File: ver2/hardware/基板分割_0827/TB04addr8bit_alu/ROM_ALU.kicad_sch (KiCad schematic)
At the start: 31 parts, among them IC601 74HC161N, J601 Conn_02x05_Odd_Even, SW601 SW_Coded_SH-7050, U601 74LS273, U602 74HC273, U603 28C256, U604 28C256, U605 74HC74, U606 74HC273, U607 74HC238

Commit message: ver2: 3分割で他基板側のICを削除(ctrl 9・alu 15・if 2個)
削除前にまたぎ本数(37/20)で割り当てを検算。kicad-cliのパース通過を確認。

Co-Authored-By: Claude Opus 5 <noreply@anthropic.com>
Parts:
- removed IC601: 74HC161N, Package_DIP:DIP-16_W7.62mm_Socket, symbol 74HC161:74HC161N
- removed U601: 74LS273, Package_DIP:DIP-20_W7.62mm_Socket, symbol 74xx:74LS273
- removed U602, U606: 74HC273, Package_DIP:DIP-20_W7.62mm_Socket, symbol 74xx:74HC273
- removed U604: 28C256, Socket:DIP_Socket-28_W11.9mm_W12.7mm_W15.24mm_W17.78mm_W18.5mm_3M_228-1277-00-0602J, symbol Memory_EEPROM:28C256
- removed U607: 74HC238, Package_DIP:DIP-16_W7.62mm_Socket, symbol 74xx:74HC238

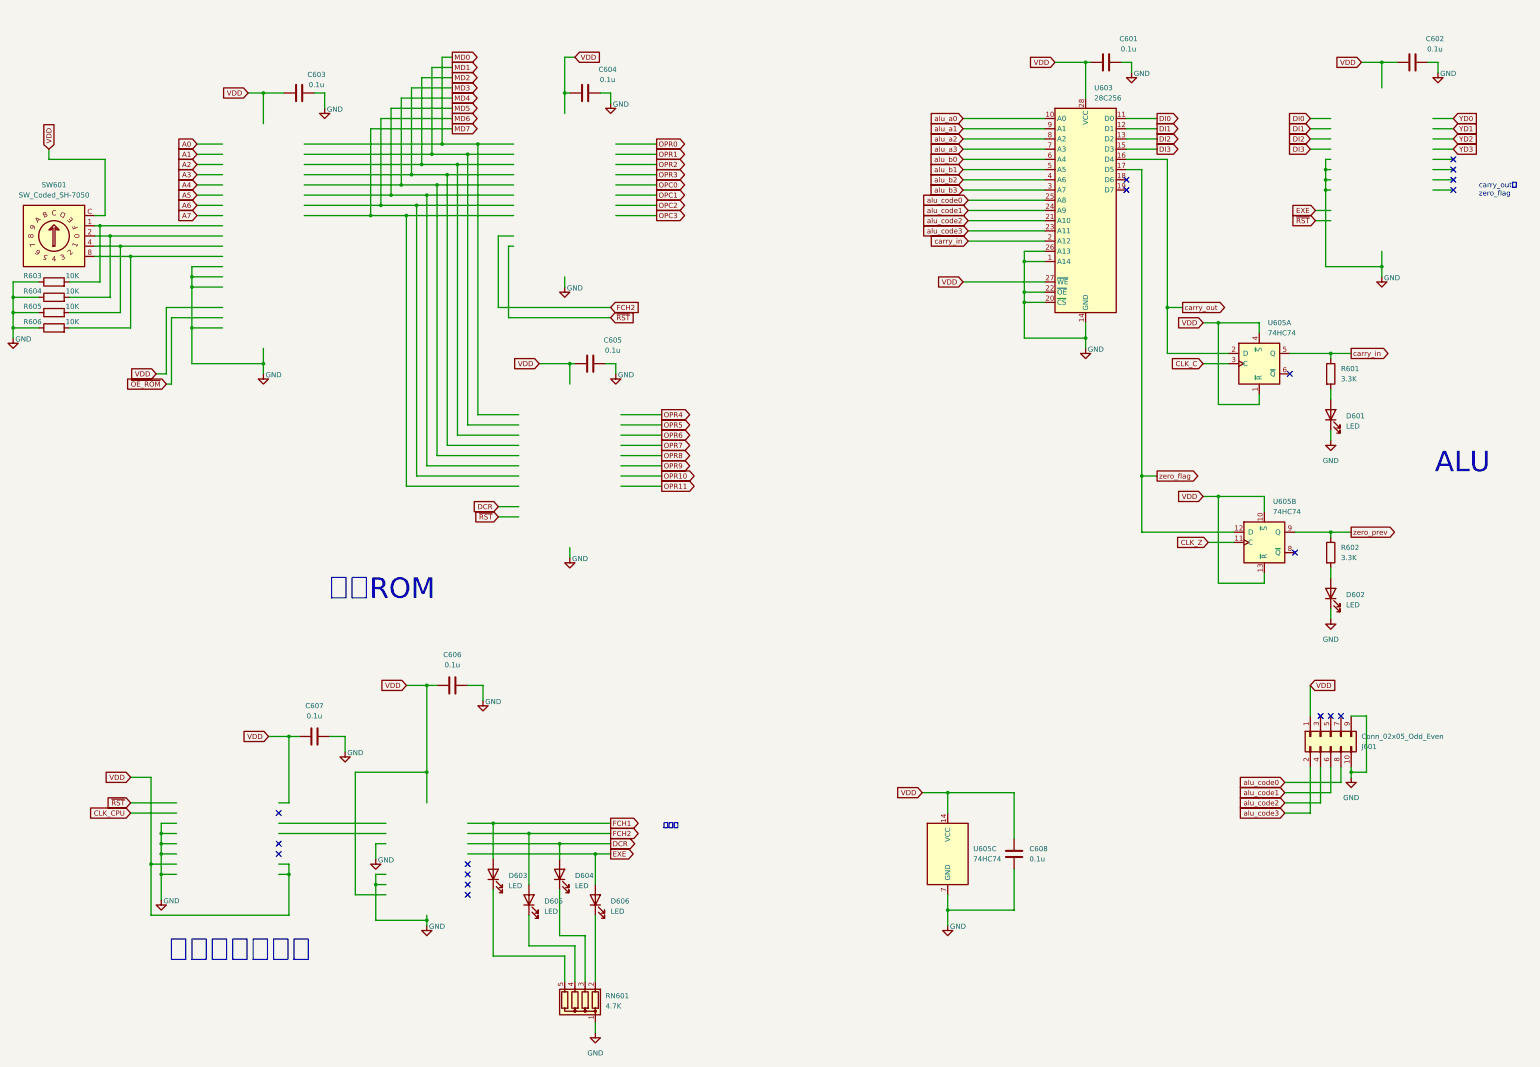
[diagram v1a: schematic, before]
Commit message: ver2: 3分割でシート内の不要部品・配線を削除(検証合格)／キャリアを0827へコピー
- 制御34・演算25・IF10=IC69でマスターと一致、部品の取りこぼし0
- ピン-ネット署名の変化0件=誤って線を切った箇所なし
- またぐ信号は制御/演算35・IF/制御18で手順書の表と過不足ゼロ

Co-Authored-By: Claude Opus 5 <noreply@anthropic.com>
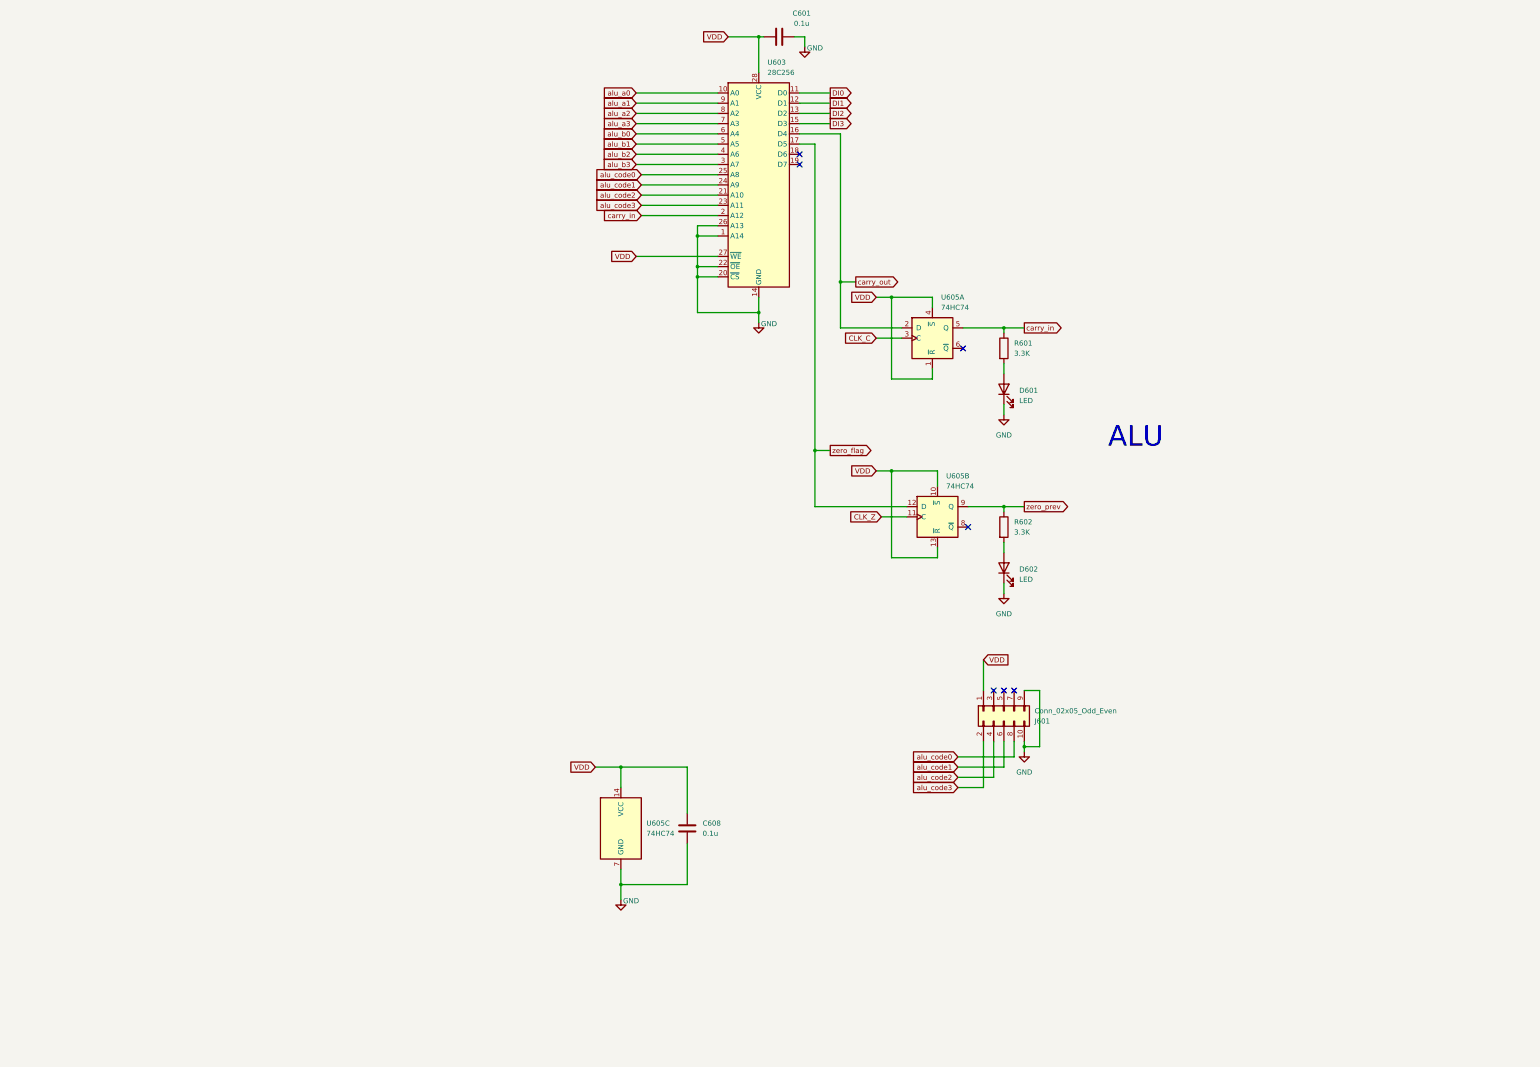
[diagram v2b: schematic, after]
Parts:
- removed C602, C603, C604, C605, C606, C607: 0.1u, Capacitor_THT:C_Disc_D4.3mm_W1.9mm_P5.00mm, symbol Device:C
- removed D603, D604, D605, D606: LED, LED_THT:LED_D3.0mm_Clear, symbol Device:LED
- removed R603, R604, R605, R606: 10K, Resistor_THT:R_Axial_DIN0207_L6.3mm_D2.5mm_P10.16mm_Horizontal, symbol Device:R
- removed RN601: 4.7K, Resistor_THT:R_Array_SIP5, symbol Device:R_Network04
- removed SW601: SW_Coded_SH-7050, Library:dip_rotary_sw, symbol Switch:SW_Coded_SH-7050
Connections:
- no-connect marks 18 -> 7
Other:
- note removed: "carry_outと zero_flag"
- note removed: "フェーズ発生器"
- note removed: "命令ROM"
- note removed: "正論理"
- moved on the sheet: C601, C608, D601, D602, J601, R601, R602, U603, U605A, U605B, U605C
